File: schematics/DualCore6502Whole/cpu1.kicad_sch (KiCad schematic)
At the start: 7 parts, among them U2 W65C02S, U3 74HC157

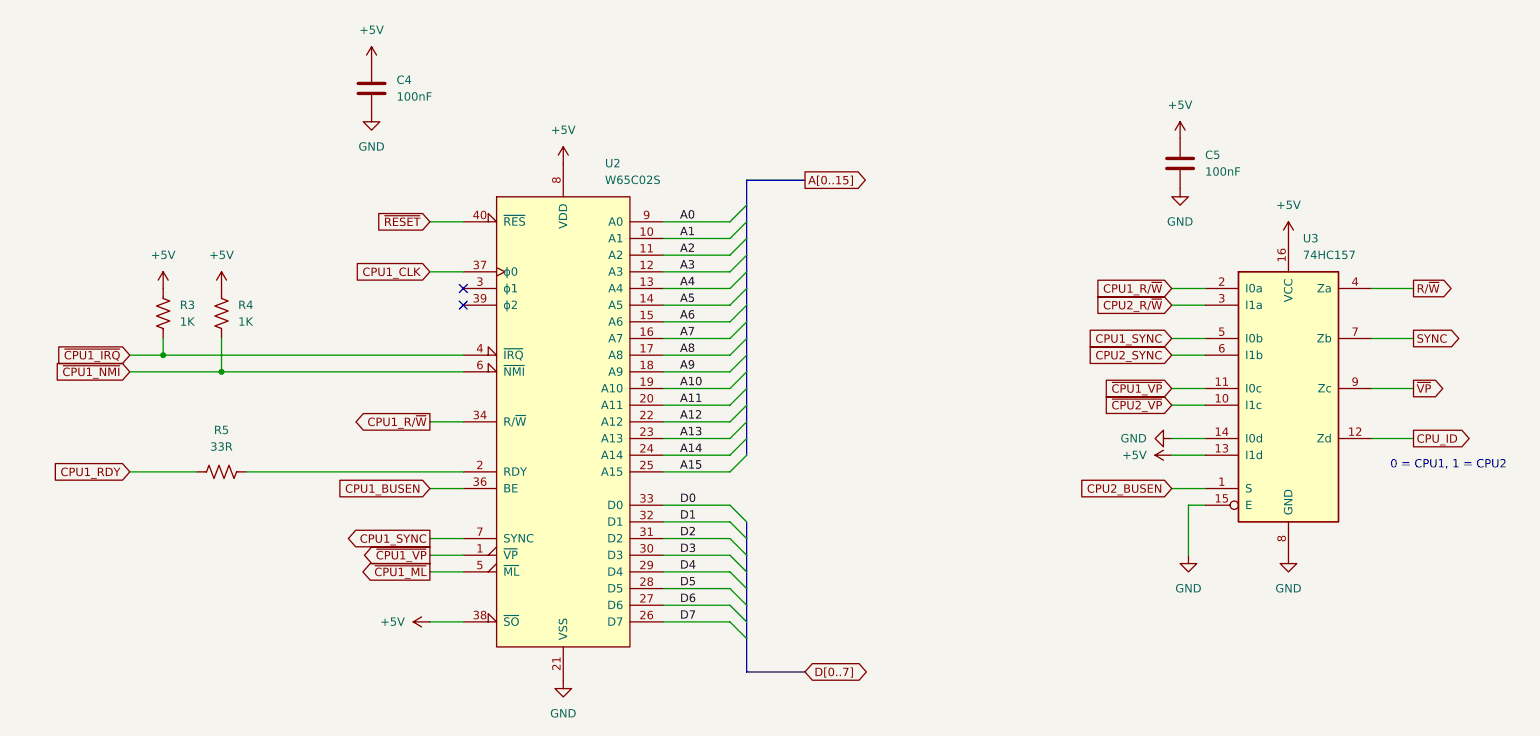
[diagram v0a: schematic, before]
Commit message: Remove the need to multiplex the control lines
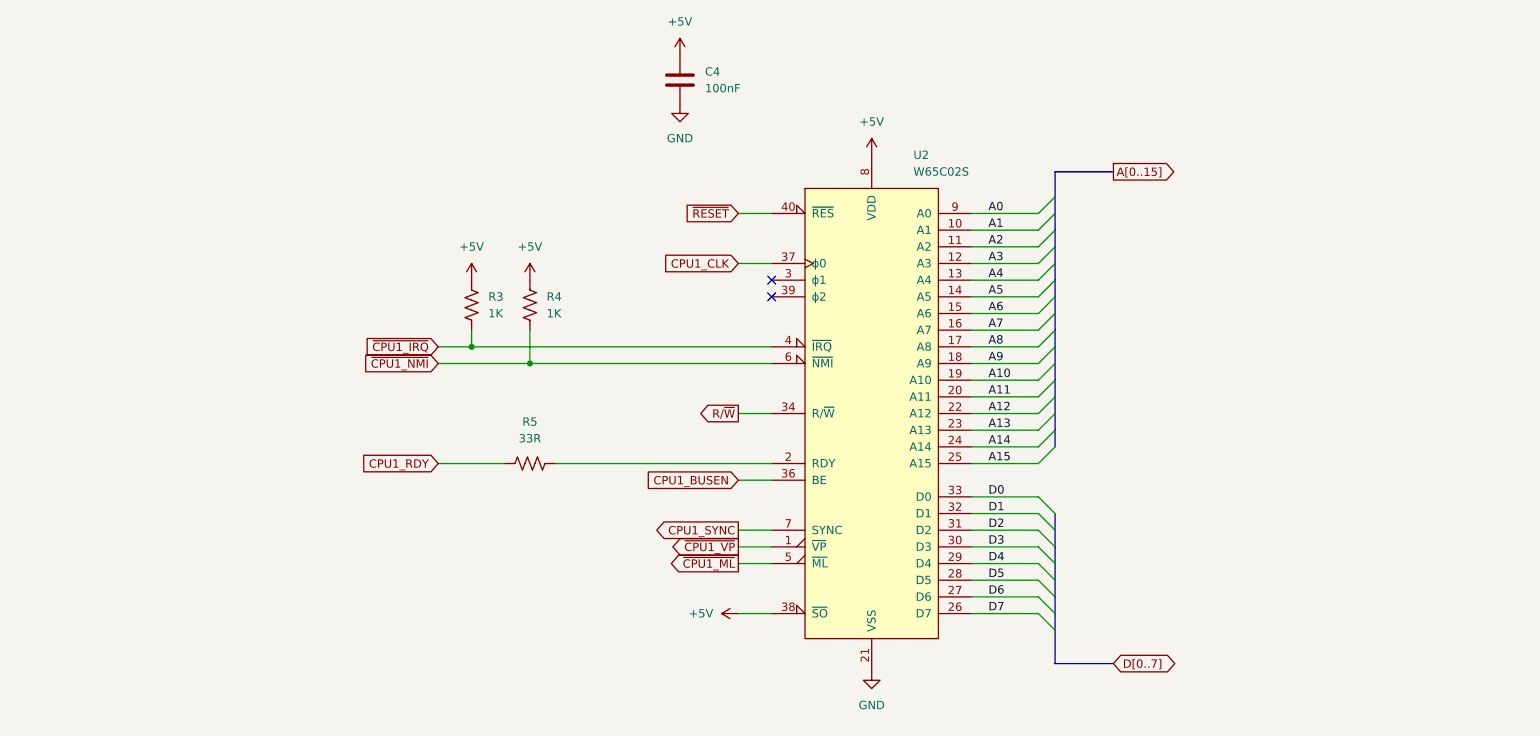
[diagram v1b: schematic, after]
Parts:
- removed C5: 100nF, Capacitor_THT:C_Disc_D5.0mm_W2.5mm_P5.00mm, symbol Device:C
- removed U3: 74HC157, Package_DIP:DIP-16_W7.62mm, symbol 74xx:74LS157
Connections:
- net CPU1_R/~{W} is gone; now on net R/~{W}: U2.34 (R/~{W})
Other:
- note removed: "0 = CPU1, 1 = CPU2"
- moved on the sheet: C4, R3, R4, R5, U2

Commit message: Update the schematic
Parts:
- R5: value 33R -> 1K; footprint (none) -> Resistor_THT:R_Axial_DIN0207_L6.3mm_D2.5mm_P10.16mm_Horizontal
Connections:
- net CPU1_RDY is gone; now on net +5V: R5.1
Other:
- title: (none) -> Dual Core 65C02 Computer
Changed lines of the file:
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@@
 	(generator_version "8.0")
 	(paper "A4")
+	(title_block
+		(title "Dual Core 65C02 Computer")
+		(date "2026")
+		(comment 1 "Copyright (c) 2026 Rhys Weatherley")
+		(comment 3 "CPU 1")
+	)
 	(junction
 		(at 90.17 83.82)
@@
 	(wire
 		(pts
-			(xy 102.87 101.6) (xy 135.89 101.6)
-		)
-		(stroke
-			(width 0)
-			(type default)
-		)
-	)
-	(wire
-		(pts
 			(xy 166.37 88.9) (xy 176.53 88.9)
 		)
@@
 		)
 	)
+	(wire
+		(pts
+			(xy 107.95 81.28) (xy 107.95 101.6)
+		)
+		(stroke
+			(width 0)
+			(type default)
+		)
+	)
 	(bus
 		(pts
@@
 		)
 	)
+	(wire
+		(pts
+			(xy 107.95 101.6) (xy 135.89 101.6)
+		)
+		(stroke
+			(width 0)
+			(type default)
+		)
+	)
 	(bus
 		(pts
@@
 		(pts
 			(xy 166.37 109.22) (xy 176.53 109.22)
-		)
-		(stroke
-			(width 0)
-			(type default)
-		)
-	)
-	(wire
-		(pts
-			(xy 85.09 101.6) (xy 95.25 101.6)
 		)
 		(stroke
@@
 		(property "Intersheetrefs" "${INTERSHEET_REFS}"
 			(at 72.8519 83.82 0)
-			(effects
-				(font
-					(size 1.27 1.27)
-				)
-				(justify right)
-				(hide yes)
-			)
-		)
-	)
-	(global_label "CPU1_RDY"
-		(shape input)
-		(at 85.09 101.6 180)
-		(fields_autoplaced yes)
-		(effects
-			(font
-				(size 1.27 1.27)
-			)
-			(justify right)
-		)
-		(property "Intersheetrefs" "${INTERSHEET_REFS}"
-			(at 72.4286 101.6 0)
 			(effects
 				(font
@@
 		(dnp no)
 		(fields_autoplaced yes)
-		(property "Reference" "#PWR20"
+		(property "Reference" "#PWR21"
 			(at 151.13 139.7 0)
 			(effects
@@
 			(project ""
 				(path "/93e0914e-b2e9-49c2-95f2-7cc419f4ea20/3e6d4e37-17a2-42ed-9829-cf500e89d60f"
-					(reference "#PWR20")
+					(reference "#PWR21")
+					(unit 1)
+				)
+			)
+		)
+	)
+	(symbol
+		(lib_id "Device:R_US")
+		(at 107.95 77.47 0)
+		(unit 1)
+		(exclude_from_sim no)
+		(in_bom yes)
+		(on_board yes)
+		(dnp no)
+		(fields_autoplaced yes)
+		(property "Reference" "R5"
+			(at 110.49 76.1999 0)
+			(effects
+				(font
+					(size 1.27 1.27)
+				)
+				(justify left)
+			)
+		)
+		(property "Value" "1K"
+			(at 110.49 78.7399 0)
+			(effects
+				(font
+					(size 1.27 1.27)
+				)
+				(justify left)
+			)
+		)
+		(property "Footprint" "Resistor_THT:R_Axial_DIN0207_L6.3mm_D2.5mm_P10.16mm_Horizontal"
+			(at 108.966 77.724 90)
+			(effects
+				(font
+					(size 1.27 1.27)
+				)
+				(hide yes)
+			)
+		)
+		(property "Datasheet" "~"
+			(at 107.95 77.47 0)
+			(effects
+				(font
+					(size 1.27 1.27)
+				)
+				(hide yes)
+			)
+		)
+		(property "Description" "Resistor, US symbol"
+			(at 107.95 77.47 0)
+			(effects
+				(font
+					(size 1.27 1.27)
+				)
+				(hide yes)
+			)
+		)
+		(pin "2"
+		)
+		(pin "1"
+		)
+		(instances
+			(project "DualCore6502Whole"
+				(path "/93e0914e-b2e9-49c2-95f2-7cc419f4ea20/3e6d4e37-17a2-42ed-9829-cf500e89d60f"
+					(reference "R5")
+					(unit 1)
+				)
+			)
+		)
+	)
+	(symbol
+		(lib_id "power:+5V")
+		(at 107.95 73.66 0)
+		(unit 1)
+		(exclude_from_sim no)
+		(in_bom yes)
+		(on_board yes)
+		(dnp no)
+		(fields_autoplaced yes)
+		(property "Reference" "#PWR16"
+			(at 107.95 77.47 0)
+			(effects
+				(font
+					(size 1.27 1.27)
+				)
+				(hide yes)
+			)
+		)
+		(property "Value" "+5V"
+			(at 107.95 68.58 0)
+			(effects
+				(font
+					(size 1.27 1.27)
+				)
+			)
+		)
+		(property "Footprint" ""
+			(at 107.95 73.66 0)
+			(effects
+				(font
+					(size 1.27 1.27)
+				)
+				(hide yes)
+			)
+		)
+		(property "Datasheet" ""
+			(at 107.95 73.66 0)
+			(effects
+				(font
+					(size 1.27 1.27)
+				)
+				(hide yes)
+			)
+		)
+		(property "Description" "Power symbol creates a global label with name \"+5V\""
+			(at 107.95 73.66 0)
+			(effects
+				(font
+					(size 1.27 1.27)
+				)
+				(hide yes)
+			)
+		)
+		(pin "1"
+		)
+		(instances
+			(project "DualCore6502Whole"
+				(path "/93e0914e-b2e9-49c2-95f2-7cc419f4ea20/3e6d4e37-17a2-42ed-9829-cf500e89d60f"
+					(reference "#PWR16")
 					(unit 1)
 				)
@@
 		(dnp no)
 		(fields_autoplaced yes)
-		(property "Reference" "#PWR17"
+		(property "Reference" "#PWR18"
 			(at 121.92 53.34 0)
 			(effects
@@
 			(project "DualCore6502Whole"
 				(path "/93e0914e-b2e9-49c2-95f2-7cc419f4ea20/3e6d4e37-17a2-42ed-9829-cf500e89d60f"
-					(reference "#PWR17")
+					(reference "#PWR18")
 					(unit 1)
 				)
@@
 		(dnp no)
 		(fields_autoplaced yes)
-		(property "Reference" "#PWR18"
+		(property "Reference" "#PWR19"
 			(at 134.62 124.46 0)
 			(effects
@@
 			(project "DualCore6502Whole"
 				(path "/93e0914e-b2e9-49c2-95f2-7cc419f4ea20/3e6d4e37-17a2-42ed-9829-cf500e89d60f"
-					(reference "#PWR18")
+					(reference "#PWR19")
 					(unit 1)
 				)
@@
 		(dnp no)
 		(fields_autoplaced yes)
-		(property "Reference" "#PWR19"
+		(property "Reference" "#PWR20"
 			(at 151.13 58.42 0)
 			(effects
@@
 			(project ""
 				(path "/93e0914e-b2e9-49c2-95f2-7cc419f4ea20/3e6d4e37-17a2-42ed-9829-cf500e89d60f"
-					(reference "#PWR19")
+					(reference "#PWR20")
 					(unit 1)
 				)
@@
 		(dnp no)
 		(fields_autoplaced yes)
-		(property "Reference" "#PWR16"
+		(property "Reference" "#PWR17"
 			(at 121.92 43.18 0)
 			(effects
@@
 			(project "DualCore6502Whole"
 				(path "/93e0914e-b2e9-49c2-95f2-7cc419f4ea20/3e6d4e37-17a2-42ed-9829-cf500e89d60f"
-					(reference "#PWR16")
+					(reference "#PWR17")
 					(unit 1)
 				)
-			)
-		)
-	)
-	(symbol
-		(lib_id "Device:R_US")
-		(at 99.06 101.6 90)
-		(unit 1)
-		(exclude_from_sim no)
-		(in_bom yes)
-		(on_board yes)
-		(dnp no)
-		(fields_autoplaced yes)
-		(property "Reference" "R5"
-			(at 99.06 95.25 90)
-			(effects
-				(font
-					(size 1.27 1.27)
-				)
-			)
-		)
-		(property "Value" "33R"
-			(at 99.06 97.79 90)
-			(effects
-				(font
-					(size 1.27 1.27)
-				)
-			)
-		)
-		(property "Footprint" ""
-			(at 99.314 100.584 90)
-			(effects
-				(font
-					(size 1.27 1.27)
-				)
-				(hide yes)
-			)
-		)
-		(property "Datasheet" "~"
-			(at 99.06 101.6 0)
-			(effects
-				(font
-					(size 1.27 1.27)
-				)
-				(hide yes)
-			)
-		)
-		(property "Description" "Resistor, US symbol"
-			(at 99.06 101.6 0)
-			(effects
-				(font
-					(size 1.27 1.27)
-				)
-				(hide yes)
-			)
-		)
-		(pin "1"
-		)
-		(pin "2"
-		)
-		(instances
-			(project ""
-				(path "/93e0914e-b2e9-49c2-95f2-7cc419f4ea20/3e6d4e37-17a2-42ed-9829-cf500e89d60f"
-					(reference "R5")
-					(unit 1)
-				)

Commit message: Basic PCB layout
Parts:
- added TP1: CPU1 SYNC, TestPoint:TestPoint_Pad_D1.5mm, symbol Connector:TestPoint
- added TP2: ~{CPU1_VP}, TestPoint:TestPoint_Pad_D1.5mm, symbol Connector:TestPoint
- added TP3: ~{CPU1_ML}, TestPoint:TestPoint_Pad_D1.5mm, symbol Connector:TestPoint
- U1: renamed from U2; footprint Package_DIP:DIP-40_W15.24mm -> Package_DIP:DIP-40_W15.24mm_Socket
- renumbered C4 to C3
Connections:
- net CPU1_SYNC: no longer names the net of U1.7 (SYNC)
- net CPU1_SYNC: now also TP1.1
- net ~{CPU1_ML}: no longer names the net of U1.5 (~{ML})
- net ~{CPU1_ML}: now also TP3.1
- net ~{CPU1_VP}: no longer names the net of U1.1 (~{VP})
- net ~{CPU1_VP}: now also TP2.1
